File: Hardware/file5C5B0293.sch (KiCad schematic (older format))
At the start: 27 parts, among them J16 Conn_01x06_Male, J17 Conn_ARM_JTAG_SWD_10, J24 Digital_Connector, J25 CV_Connector, J26 Pot_Connector, J27 Attenuverter_Connector, U13 STM32F303RBTx

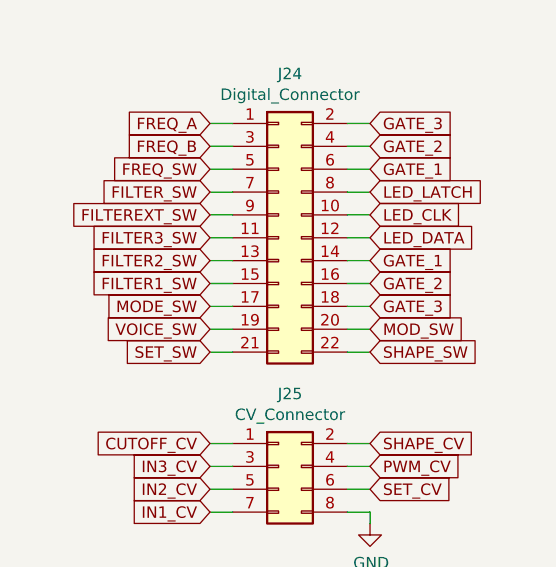
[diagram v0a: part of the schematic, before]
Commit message: Added some connector routing
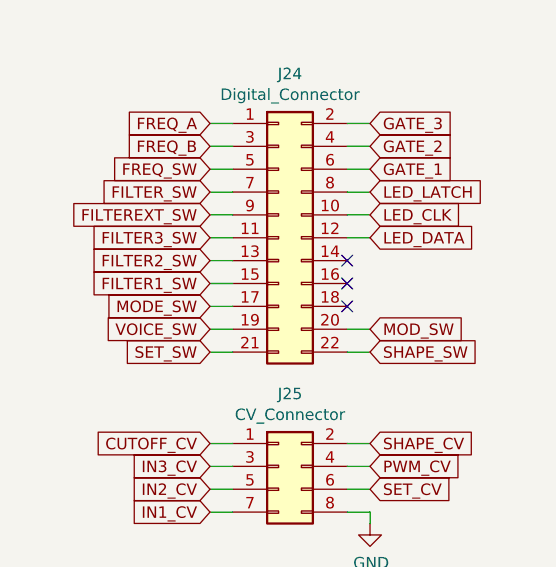
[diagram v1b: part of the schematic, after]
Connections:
- net GATE_1: no longer J24.14 (Pin_14)
- net GATE_2: no longer J24.16 (Pin_16)
- net GATE_3: no longer J24.18 (Pin_18)
- no-connect marks 13 -> 16
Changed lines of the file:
@@
 Text GLabel 9300 2050 0    50   Input ~ 0
 FREQ_B
-Text GLabel 10000 2750 2    50   Input ~ 0
-GATE_3
-Text GLabel 10000 2650 2    50   Input ~ 0
-GATE_2
-Text GLabel 10000 2550 2    50   Input ~ 0
-GATE_1
 Text GLabel 10000 2450 2    50   Input ~ 0
 LED_DATA
@@
 Wire Wire Line
 	9900 2850 10000 2850
-Wire Wire Line
-	9900 2750 10000 2750
-Wire Wire Line
-	9900 2650 10000 2650
-Wire Wire Line
-	9900 2550 10000 2550
 Wire Wire Line
 	9900 2450 10000 2450
@@
 Wire Wire Line
 	9300 5050 9400 5050
+NoConn ~ 9900 2550
+NoConn ~ 9900 2650
+NoConn ~ 9900 2750
 $EndSCHEMATC

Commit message: STM32CubeMX Blinky
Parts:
- C63: symbol Device:C -> Device:CP
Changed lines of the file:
@@
 $EndComp
 $Comp
-L Device:C C63
+L Device:CP C63
 U 1 1 5BEF067C
 P 1750 6100

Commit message: IT WORKS
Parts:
- removed J17: Conn_ARM_JTAG_SWD_10, Connector_PinHeader_2.54mm:PinHeader_2x05_P2.54mm_Vertical, symbol Connector:Conn_ARM_JTAG_SWD_10
- added J17: Conn_01x03_Male, Connector_PinHeader_2.54mm:PinHeader_1x03_P2.54mm_Vertical, symbol Connector:Conn_01x03_Male
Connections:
- net +3V3: now also J16.1 (Pin_1)
- net GND: now also J16.3 (Pin_3), J17.3 (Pin_3); no longer J16.1 (Pin_1)
- net RESET: now also J16.5 (Pin_5)
- net RX: now also J17.2 (Pin_2); no longer J16.4 (Pin_4)
- net SWCLK: now also J16.2 (Pin_2)
- net SWDIO: now also J16.4 (Pin_4)
- net TX: now also J17.1 (Pin_1); no longer J16.5 (Pin_5)
- no-connect marks 16 -> 11
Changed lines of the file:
@@
 Wire Wire Line
 	1500 5750 1500 5800
-$Comp
-L power:GND #PWR0137
-U 1 1 5BF2206A
-P 1900 3050
-F 0 "#PWR0137" H 1900 2800 50  0001 C CNN
-F 1 "GND" H 1905 2877 50  0000 C CNN
-F 2 "" H 1900 3050 50  0001 C CNN
-F 3 "" H 1900 3050 50  0001 C CNN
-	1    1900 3050
-	1    0    0    -1
-$EndComp
 Wire Wire Line
 	1500 5800 1250 5800
@@
 	5250 7450 5550 7450
 $Comp
-L Connector:Conn_ARM_JTAG_SWD_10 J17
-U 1 1 5BF86C4D
-P 1950 2250
-F 0 "J17" H 1510 2296 50  0000 R CNN
-F 1 "Conn_ARM_JTAG_SWD_10" H 1510 2205 50  0000 R CNN
-F 2 "Connector_PinHeader_2.54mm:PinHeader_2x05_P2.54mm_Vertical" H 2000 1700 50  0001 L TNN
-F 3 "http://infocenter.arm.com/help/topic/com.arm.doc.faqs/attached/13634/cortex_debug_connectors.pdf" V 1600 1000 50  0001 C CNN
-	1    1950 2250
-	1    0    0    -1
-$EndComp
-Wire Wire Line
-	1900 3050 1900 2950
-Wire Wire Line
-	1900 2950 1850 2950
-Wire Wire Line
-	1850 2950 1850 2850
-Wire Wire Line
-	1950 2850 1950 2950
-Wire Wire Line
-	1950 2950 1900 2950
-Connection ~ 1900 2950
-$Comp
 L power:+3.3V #PWR0138
 U 1 1 5BF90955
-P 1950 1600
-F 0 "#PWR0138" H 1950 1450 50  0001 C CNN
-F 1 "+3.3V" H 1965 1773 50  0000 C CNN
-F 2 "" H 1950 1600 50  0001 C CNN
-F 3 "" H 1950 1600 50  0001 C CNN
-	1    1950 1600
-	1    0    0    -1
-$EndComp
-Wire Wire Line
-	1950 1600 1950 1650
-Text GLabel 2600 1950 2    50   Input ~ 0
+P 2350 1750
+F 0 "#PWR0138" H 2350 1600 50  0001 C CNN
+F 1 "+3.3V" H 2365 1923 50  0000 C CNN
+F 2 "" H 2350 1750 50  0001 C CNN
+F 3 "" H 2350 1750 50  0001 C CNN
+	1    2350 1750
+	1    0    0    -1
+$EndComp
+Text GLabel 2800 1850 2    50   Input ~ 0
 RESET
-Wire Wire Line
-	2600 1950 2450 1950
 Text GLabel 6500 3150 2    50   Input ~ 0
 SET_SW
 Text GLabel 6500 3350 2    50   Input ~ 0
 SWCLK
-Text GLabel 2600 2250 2    50   Input ~ 0
+Text GLabel 2350 2250 2    50   Input ~ 0
 SWDIO
-Wire Wire Line
-	2600 2250 2450 2250
-Text GLabel 2600 2150 2    50   Input ~ 0
+Text GLabel 2350 2050 2    50   Input ~ 0
 SWCLK
-Wire Wire Line
-	2600 2150 2450 2150
-$Comp
-L Connector:Conn_01x06_Male J16
-U 1 1 5BFB55EB
-P 1850 3800
-F 0 "J16" H 1822 3680 50  0000 R CNN
-F 1 "Conn_01x06_Male" H 1822 3771 50  0000 R CNN
-F 2 "Connector_PinHeader_2.54mm:PinHeader_1x06_P2.54mm_Vertical" H 1850 3800 50  0001 C CNN
-F 3 "~" H 1850 3800 50  0001 C CNN
-	1    1850 3800
-	1    0    0    1
-$EndComp
 Text GLabel 6500 2850 2    50   Input ~ 0
 TX
 Text GLabel 6500 2950 2    50   Input ~ 0
 RX
-Text GLabel 2200 3600 2    50   Input ~ 0
+Text GLabel 2100 4500 2    50   Input ~ 0
 TX
-Wire Wire Line
-	2200 3600 2050 3600
-Text GLabel 2200 3700 2    50   Input ~ 0
+Text GLabel 2100 4600 2    50   Input ~ 0
 RX
-Wire Wire Line
-	2200 3700 2050 3700
 $Comp
 L power:GND #PWR0139
 U 1 1 5BFD1A9D
-P 2200 4050
-F 0 "#PWR0139" H 2200 3800 50  0001 C CNN
-F 1 "GND" H 2205 3877 50  0000 C CNN
-F 2 "" H 2200 4050 50  0001 C CNN
-F 3 "" H 2200 4050 50  0001 C CNN
-	1    2200 4050
-	1    0    0    -1
-$EndComp
-Wire Wire Line
-	2200 4050 2200 4000
-Wire Wire Line
-	2200 4000 2050 4000
-NoConn ~ 2050 3500
-NoConn ~ 2050 3800
-NoConn ~ 2050 3900
-NoConn ~ 2450 2350
-NoConn ~ 2450 2450
+P 2100 4750
+F 0 "#PWR0139" H 2100 4500 50  0001 C CNN
+F 1 "GND" H 2105 4577 50  0000 C CNN
+F 2 "" H 2100 4750 50  0001 C CNN
+F 3 "" H 2100 4750 50  0001 C CNN
+	1    2100 4750
+	1    0    0    -1
+$EndComp
 Text GLabel 4200 4050 0    50   Input ~ 0
 SET_ATTEN
@@
 NoConn ~ 9900 2650
 NoConn ~ 9900 2750
+$Comp
+L Connector:Conn_01x03_Male J17
+U 1 1 5C9CB1BC
+P 1800 4600
+F 0 "J17" H 1906 4878 50  0000 C CNN
+F 1 "Conn_01x03_Male" H 1906 4787 50  0000 C CNN
+F 2 "Connector_PinHeader_2.54mm:PinHeader_1x03_P2.54mm_Vertical" H 1800 4600 50  0001 C CNN
+F 3 "~" H 1800 4600 50  0001 C CNN
+	1    1800 4600
+	1    0    0    -1
+$EndComp
+Wire Wire Line
+	2100 4750 2100 4700
+Wire Wire Line
+	2100 4700 2000 4700
+Wire Wire Line
+	2100 4600 2000 4600
+Wire Wire Line
+	2100 4500 2000 4500
+$Comp
+L Connector:Conn_01x06_Male J16
+U 1 1 5CA02872
+P 1800 2150
+F 0 "J16" H 1906 2528 50  0000 C CNN
+F 1 "Conn_01x06_Male" H 1906 2437 50  0000 C CNN
+F 2 "Connector_PinHeader_2.54mm:PinHeader_1x06_P2.54mm_Vertical" H 1800 2150 50  0001 C CNN
+F 3 "~" H 1800 2150 50  0001 C CNN
+	1    1800 2150
+	1    0    0    -1
+$EndComp
+Wire Wire Line
+	2000 1950 2350 1950
+Wire Wire Line
+	2350 1950 2350 1750
+Wire Wire Line
+	2350 2050 2000 2050
+$Comp
+L power:GND #PWR0163
+U 1 1 5CA355D8
+P 2750 2200
+F 0 "#PWR0163" H 2750 1950 50  0001 C CNN
+F 1 "GND" H 2755 2027 50  0000 C CNN
+F 2 "" H 2750 2200 50  0001 C CNN
+F 3 "" H 2750 2200 50  0001 C CNN
+	1    2750 2200
+	1    0    0    -1
+$EndComp
+Wire Wire Line
+	2750 2200 2750 2150
+Wire Wire Line
+	2750 2150 2000 2150
+Wire Wire Line
+	2350 2250 2000 2250
+Text GLabel 2350 2350 2    50   Input ~ 0
+RESET
+Wire Wire Line
+	2350 2350 2000 2350
 $EndSCHEMATC

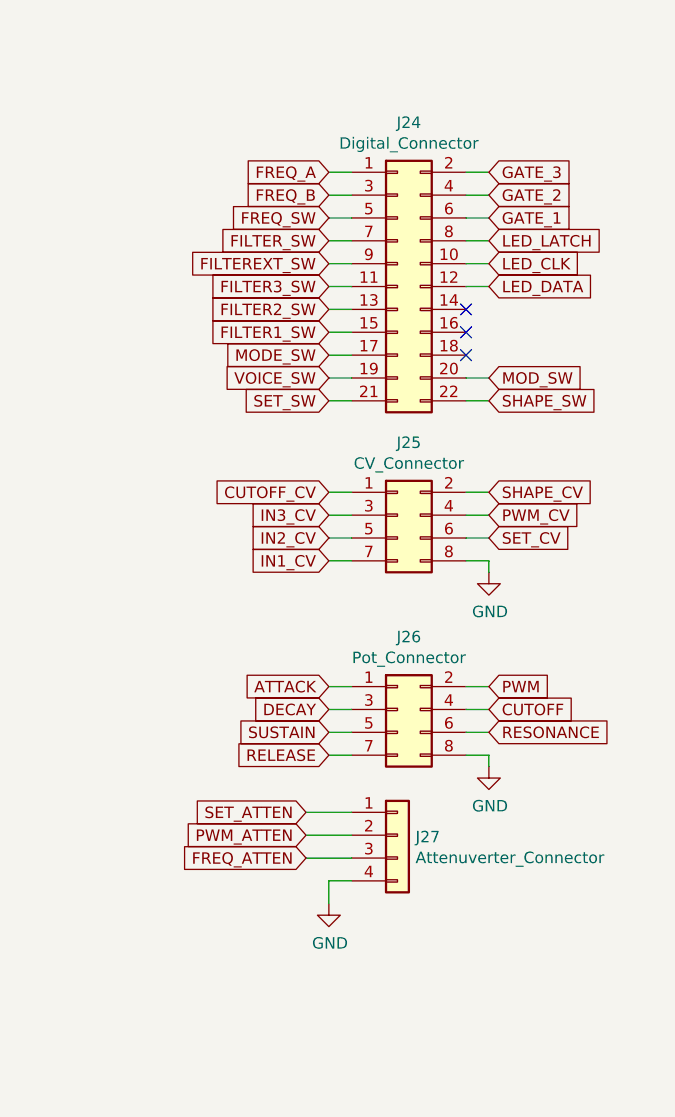
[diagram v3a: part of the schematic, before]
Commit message: Updated to single four layer board
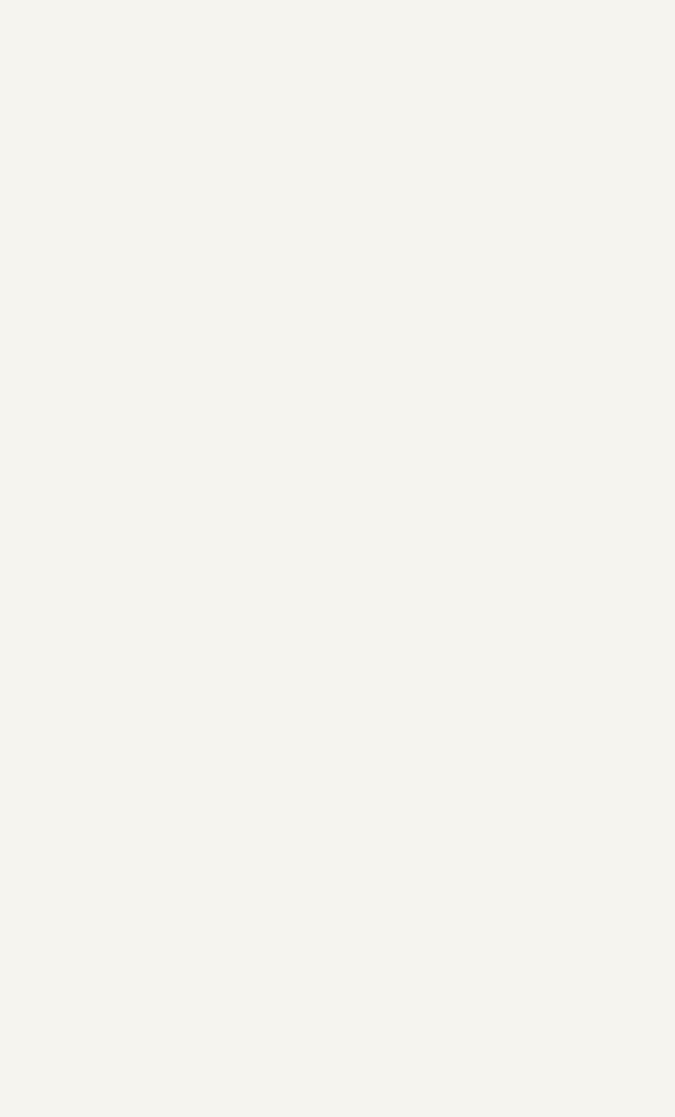
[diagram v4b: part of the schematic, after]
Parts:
- removed J24: Digital_Connector, Connector_PinHeader_2.54mm:PinHeader_2x11_P2.54mm_Vertical, symbol Connector_Generic:Conn_02x11_Odd_Even
- removed J25: CV_Connector, Connector_PinSocket_2.54mm:PinSocket_2x04_P2.54mm_Vertical, symbol Connector_Generic:Conn_02x04_Odd_Even
- removed J26: Pot_Connector, Connector_PinSocket_2.54mm:PinSocket_2x04_P2.54mm_Vertical, symbol Connector_Generic:Conn_02x04_Odd_Even
- removed J27: Attenuverter_Connector, Connector_PinSocket_2.54mm:PinSocket_1x04_P2.54mm_Vertical, symbol Connector_Generic:Conn_01x04
- J16: footprint Connector_PinHeader_2.54mm:PinHeader_1x06_P2.54mm_Vertical -> Connector_PinSocket_2.54mm:PinSocket_1x06_P2.54mm_Vertical_SMD_Pin1Left
- J17: footprint Connector_PinHeader_2.54mm:PinHeader_1x03_P2.54mm_Vertical -> Connector_PinSocket_2.54mm:PinSocket_1x03_P2.54mm_Vertical_SMD_Pin1Left
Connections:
- no-connect marks 11 -> 8
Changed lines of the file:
@@
 Connection ~ 5500 5650
 NoConn ~ 5200 1750
-Text GLabel 9300 1950 0    50   Input ~ 0
-FREQ_A
-Text GLabel 9300 2050 0    50   Input ~ 0
-FREQ_B
-Text GLabel 10000 2450 2    50   Input ~ 0
-LED_DATA
-Text GLabel 10000 2350 2    50   Input ~ 0
-LED_CLK
-Text GLabel 10000 2250 2    50   Input ~ 0
-LED_LATCH
-Text GLabel 10000 2150 2    50   Input ~ 0
-GATE_1
-Text GLabel 10000 2050 2    50   Input ~ 0
-GATE_2
-Text GLabel 10000 1950 2    50   Input ~ 0
-GATE_3
-Text GLabel 9300 2150 0    50   Input ~ 0
-FREQ_SW
-Text GLabel 9300 2250 0    50   Input ~ 0
-FILTER_SW
-Text GLabel 9300 2350 0    50   Input ~ 0
-FILTEREXT_SW
-Text GLabel 9300 2450 0    50   Input ~ 0
-FILTER3_SW
-Text GLabel 9300 2550 0    50   Input ~ 0
-FILTER2_SW
-Text GLabel 10000 2850 2    50   Input ~ 0
-MOD_SW
-Text GLabel 9300 2750 0    50   Input ~ 0
-MODE_SW
-Text GLabel 9300 2850 0    50   Input ~ 0
-VOICE_SW
-Text GLabel 9300 2950 0    50   Input ~ 0
-SET_SW
-Text GLabel 10000 2950 2    50   Input ~ 0
-SHAPE_SW
-Text GLabel 9300 2650 0    50   Input ~ 0
-FILTER1_SW
-$Comp
-L Connector_Generic:Conn_02x11_Odd_Even J24
-U 1 1 5C3285D2
-P 9600 2450
-F 0 "J24" H 9650 3167 50  0000 C CNN
-F 1 "Digital_Connector" H 9650 3076 50  0000 C CNN
-F 2 "Connector_PinHeader_2.54mm:PinHeader_2x11_P2.54mm_Vertical" H 9600 2450 50  0001 C CNN
-F 3 "~" H 9600 2450 50  0001 C CNN
-	1    9600 2450
-	1    0    0    -1
-$EndComp
-Wire Wire Line
-	9300 1950 9400 1950
-Wire Wire Line
-	9300 2050 9400 2050
-Wire Wire Line
-	9300 2150 9400 2150
-Wire Wire Line
-	9300 2250 9400 2250
-Wire Wire Line
-	9300 2350 9400 2350
-Wire Wire Line
-	9300 2450 9400 2450
-Wire Wire Line
-	9300 2550 9400 2550
-Wire Wire Line
-	9300 2650 9400 2650
-Wire Wire Line
-	9300 2750 9400 2750
-Wire Wire Line
-	9300 2850 9400 2850
-Wire Wire Line
-	9300 2950 9400 2950
-Wire Wire Line
-	9900 2950 10000 2950
-Wire Wire Line
-	9900 2850 10000 2850
-Wire Wire Line
-	9900 2450 10000 2450
-Wire Wire Line
-	9900 2350 10000 2350
-Wire Wire Line
-	9900 2250 10000 2250
-Wire Wire Line
-	9900 2150 10000 2150
-Wire Wire Line
-	9900 2050 10000 2050
-Wire Wire Line
-	9900 1950 10000 1950
-Text GLabel 9300 3350 0    50   Input ~ 0
-CUTOFF_CV
-Text GLabel 9300 3450 0    50   Input ~ 0
-IN3_CV
-Text GLabel 9300 3550 0    50   Input ~ 0
-IN2_CV
-Text GLabel 9300 3650 0    50   Input ~ 0
-IN1_CV
-Text GLabel 10000 3550 2    50   Input ~ 0
-SET_CV
-Text GLabel 10000 3450 2    50   Input ~ 0
-PWM_CV
-Text GLabel 10000 3350 2    50   Input ~ 0
-SHAPE_CV
-Text GLabel 9300 4200 0    50   Input ~ 0
-ATTACK
-Text GLabel 9300 4300 0    50   Input ~ 0
-DECAY
-Text GLabel 9300 4400 0    50   Input ~ 0
-SUSTAIN
-Text GLabel 9300 4500 0    50   Input ~ 0
-RELEASE
-Text GLabel 9200 4750 0    50   Input ~ 0
-SET_ATTEN
-Text GLabel 9200 4850 0    50   Input ~ 0
-PWM_ATTEN
-Text GLabel 9200 4950 0    50   Input ~ 0
-FREQ_ATTEN
-Text GLabel 10000 4400 2    50   Input ~ 0
-RESONANCE
-Text GLabel 10000 4300 2    50   Input ~ 0
-CUTOFF
-Text GLabel 10000 4200 2    50   Input ~ 0
-PWM
-$Comp
-L Connector_Generic:Conn_02x04_Odd_Even J25
-U 1 1 5C42AEF9
-P 9600 3450
-F 0 "J25" H 9650 3767 50  0000 C CNN
-F 1 "CV_Connector" H 9650 3676 50  0000 C CNN
-F 2 "Connector_PinSocket_2.54mm:PinSocket_2x04_P2.54mm_Vertical" H 9600 3450 50  0001 C CNN
-F 3 "~" H 9600 3450 50  0001 C CNN
-	1    9600 3450
-	1    0    0    -1
-$EndComp
-$Comp
-L power:GND #PWR025
-U 1 1 5C444A45
-P 10000 4550
-F 0 "#PWR025" H 10000 4300 50  0001 C CNN
-F 1 "GND" H 10005 4377 50  0000 C CNN
-F 2 "" H 10000 4550 50  0001 C CNN
-F 3 "" H 10000 4550 50  0001 C CNN
-	1    10000 4550
-	1    0    0    -1
-$EndComp
-Wire Wire Line
-	10000 3700 10000 3650
-Wire Wire Line
-	10000 3650 9900 3650
-Wire Wire Line
-	9900 3550 10000 3550
-Wire Wire Line
-	9900 3450 10000 3450
-Wire Wire Line
-	9900 3350 10000 3350
-Wire Wire Line
-	9400 3350 9300 3350
-Wire Wire Line
-	9400 3450 9300 3450
-Wire Wire Line
-	9400 3550 9300 3550
-Wire Wire Line
-	9400 3650 9300 3650
-$Comp
-L Connector_Generic:Conn_02x04_Odd_Even J26
-U 1 1 5C48DB66
-P 9600 4300
-F 0 "J26" H 9650 4617 50  0000 C CNN
-F 1 "Pot_Connector" H 9650 4526 50  0000 C CNN
-F 2 "Connector_PinSocket_2.54mm:PinSocket_2x04_P2.54mm_Vertical" H 9600 4300 50  0001 C CNN
-F 3 "~" H 9600 4300 50  0001 C CNN
-	1    9600 4300
-	1    0    0    -1
-$EndComp
-Wire Wire Line
-	10000 4550 10000 4500
-Wire Wire Line
-	10000 4500 9900 4500
-$Comp
-L power:GND #PWR023
-U 1 1 5C4BCD26
-P 10000 3700
-F 0 "#PWR023" H 10000 3450 50  0001 C CNN
-F 1 "GND" H 10005 3527 50  0000 C CNN
-F 2 "" H 10000 3700 50  0001 C CNN
-F 3 "" H 10000 3700 50  0001 C CNN
-	1    10000 3700
-	1    0    0    -1
-$EndComp
-Wire Wire Line
-	9300 4200 9400 4200
-Wire Wire Line
-	9300 4300 9400 4300
-Wire Wire Line
-	9300 4400 9400 4400
-Wire Wire Line
-	9400 4500 9300 4500
-Wire Wire Line
-	10000 4200 9900 4200
-Wire Wire Line
-	10000 4300 9900 4300
-Wire Wire Line
-	10000 4400 9900 4400
-$Comp
-L Connector_Generic:Conn_01x04 J27
-U 1 1 5C50D171
-P 9600 4850
-F 0 "J27" H 9679 4842 50  0000 L CNN
-F 1 "Attenuverter_Connector" H 9679 4751 50  0000 L CNN
-F 2 "Connector_PinSocket_2.54mm:PinSocket_1x04_P2.54mm_Vertical" H 9600 4850 50  0001 C CNN
-F 3 "~" H 9600 4850 50  0001 C CNN
-	1    9600 4850
-	1    0    0    -1
-$EndComp
-Wire Wire Line
-	9400 4750 9200 4750
-Wire Wire Line
-	9200 4850 9400 4850
-Wire Wire Line
-	9400 4950 9200 4950
-$Comp
-L power:GND #PWR021
-U 1 1 5C52CCC9
-P 9300 5150
-F 0 "#PWR021" H 9300 4900 50  0001 C CNN
-F 1 "GND" H 9305 4977 50  0000 C CNN
-F 2 "" H 9300 5150 50  0001 C CNN
-F 3 "" H 9300 5150 50  0001 C CNN
-	1    9300 5150
-	1    0    0    -1
-$EndComp
-Wire Wire Line
-	9300 5150 9300 5050
-Wire Wire Line
-	9300 5050 9400 5050
-NoConn ~ 9900 2550
-NoConn ~ 9900 2650
-NoConn ~ 9900 2750
 $Comp
 L Connector:Conn_01x03_Male J17
@@
 F 0 "J17" H 1906 4878 50  0000 C CNN
 F 1 "Conn_01x03_Male" H 1906 4787 50  0000 C CNN
-F 2 "Connector_PinHeader_2.54mm:PinHeader_1x03_P2.54mm_Vertical" H 1800 4600 50  0001 C CNN
+F 2 "Connector_PinSocket_2.54mm:PinSocket_1x03_P2.54mm_Vertical_SMD_Pin1Left" H 1800 4600 50  0001 C CNN
 F 3 "~" H 1800 4600 50  0001 C CNN
 	1    1800 4600
@@
 F 0 "J16" H 1906 2528 50  0000 C CNN
 F 1 "Conn_01x06_Male" H 1906 2437 50  0000 C CNN
-F 2 "Connector_PinHeader_2.54mm:PinHeader_1x06_P2.54mm_Vertical" H 1800 2150 50  0001 C CNN
+F 2 "Connector_PinSocket_2.54mm:PinSocket_1x06_P2.54mm_Vertical_SMD_Pin1Left" H 1800 2150 50  0001 C CNN
 F 3 "~" H 1800 2150 50  0001 C CNN
 	1    1800 2150

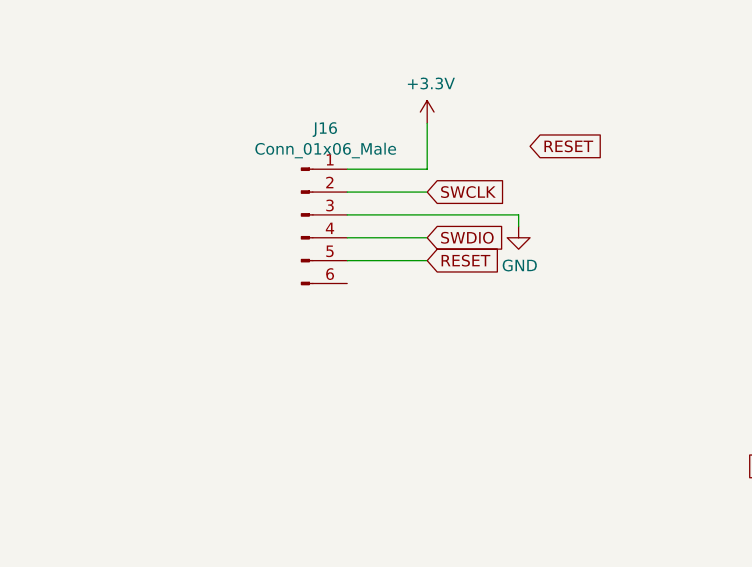
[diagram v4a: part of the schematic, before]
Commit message: Finalized 4 layer design, fixed bad opamp circuits
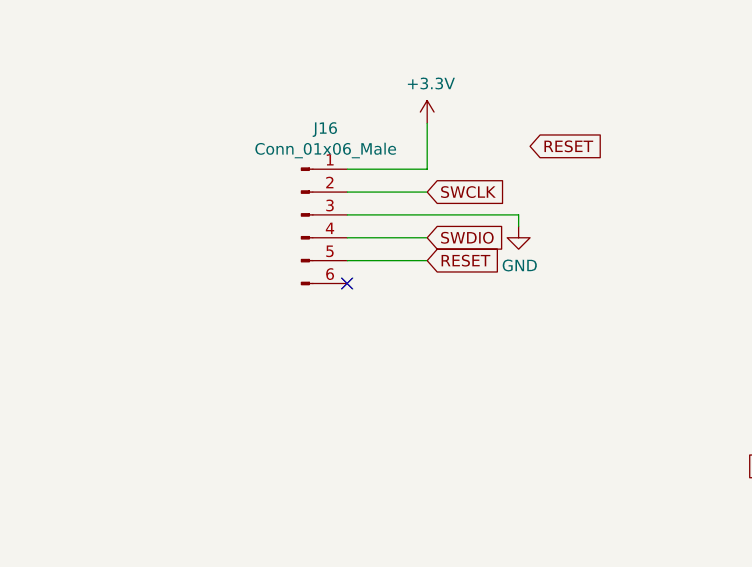
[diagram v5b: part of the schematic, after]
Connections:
- no-connect marks 8 -> 9
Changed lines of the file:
@@
 Wire Wire Line
 	2350 2350 2000 2350
+NoConn ~ 2000 2450
 $EndSCHEMATC
